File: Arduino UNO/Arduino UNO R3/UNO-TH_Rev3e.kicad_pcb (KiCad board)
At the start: 2 copper layers, 68.6 x 53.3 mm, 120 parts, among them T1 FDN340P, U1 NCP1117ST50T3G, U2 LP2985-33DBVR, U3 ATMEGA16U2-MU(R), U5 LMV358IDGKR, X1 POWERSUPPLY_DC21MMX, X2 USB-B_TH, Y1 16MHz, Y2 CSTCE16M0V53-R0 16MHZ

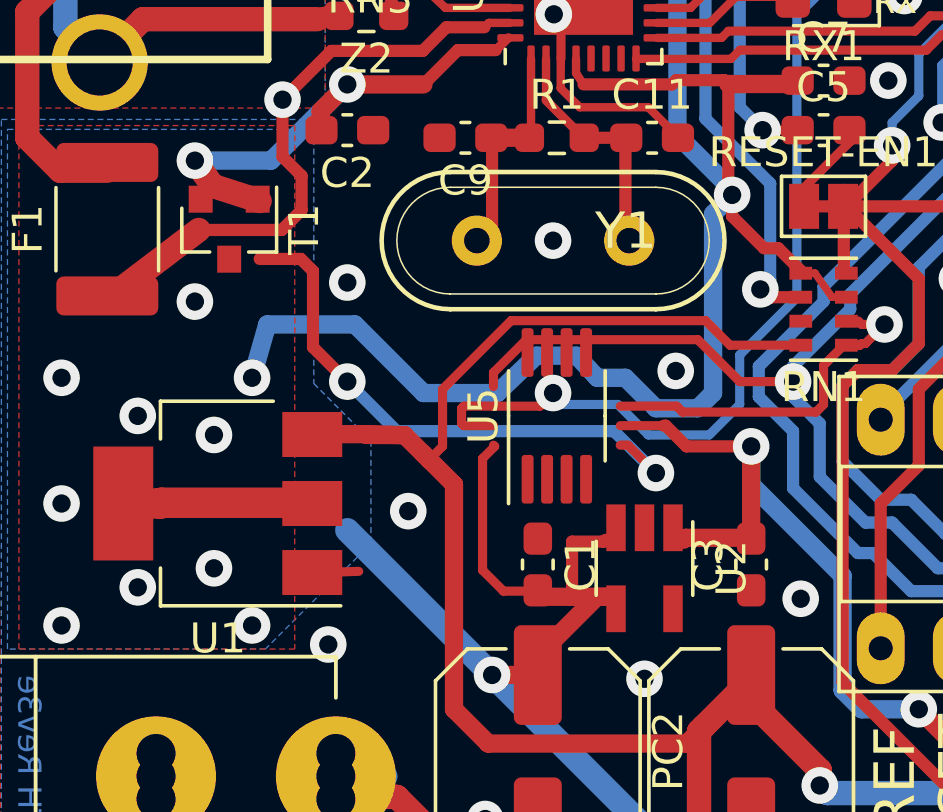
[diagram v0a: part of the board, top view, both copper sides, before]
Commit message: Reoriented some components
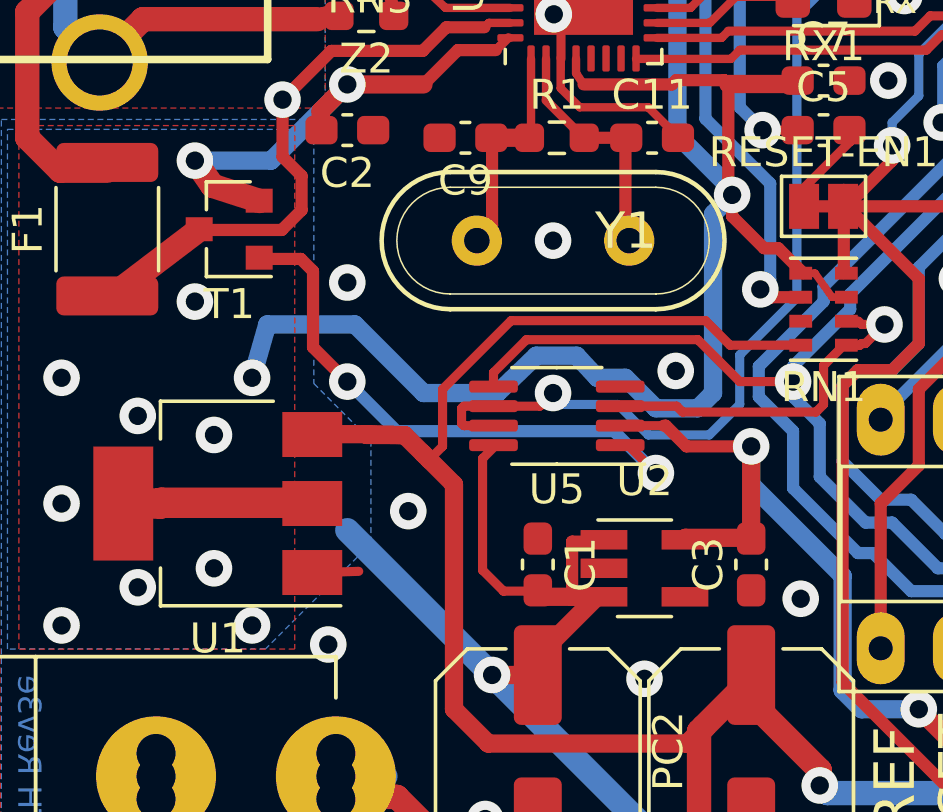
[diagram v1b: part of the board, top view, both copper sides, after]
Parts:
- turned T1 to 180 degrees
- turned U2 to 0 degrees
- turned U5 to 180 degrees
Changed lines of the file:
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@@
   )
   (footprint "Package_TO_SOT_SMD:SOT-23" (layer "F.Cu")
-    (at 122.3391 105.1306 -90)
+    (at 122.3391 105.1306 180)
     (descr "SOT-23, Standard")
     (tags "SOT-23")
     (attr smd)
-    (fp_text reference "T1" (at 0 -2.5 90) (layer "F.SilkS")
-      (effects (font (size 1 1) (thickness 0.15)))
-    )
-    (fp_text value "FDN340P" (at 0 2.5 90) (layer "F.Fab")
-      (effects (font (size 1 1) (thickness 0.15)))
-    )
-    (fp_text user "${REFERENCE}" (at 0 0) (layer "F.Fab")
+    (fp_text reference "T1" (at 0 -2.5) (layer "F.SilkS")
+      (effects (font (size 1 1) (thickness 0.15)))
+    )
+    (fp_text value "FDN340P" (at 0 2.5) (layer "F.Fab")
+      (effects (font (size 1 1) (thickness 0.15)))
+    )
+    (fp_text user "${REFERENCE}" (at 0 0 90) (layer "F.Fab")
       (effects (font (size 0.5 0.5) (thickness 0.075)))
     )
@@
     (fp_line (start -0.7 -0.95) (end -0.15 -1.52) (layer "F.Fab") (width 0.1))
     (fp_line (start -0.7 1.52) (end 0.7 1.52) (layer "F.Fab") (width 0.1))
-    (pad "1" smd rect locked (at -1 -0.95 270) (size 0.9 0.8) (layers "F.Cu" "F.Paste" "F.Mask")
+    (pad "1" smd rect locked (at -1 -0.95 180) (size 0.9 0.8) (layers "F.Cu" "F.Paste" "F.Mask")
       (net 40 "/USBVCC"))
-    (pad "2" smd rect locked (at -1 0.95 270) (size 0.9 0.8) (layers "F.Cu" "F.Paste" "F.Mask")
-      (net 1 "+5V"))
-    (pad "3" smd rect locked (at 1 0 270) (size 0.9 0.8) (layers "F.Cu" "F.Paste" "F.Mask")
+    (pad "2" smd rect locked (at -1 0.95 180) (size 0.9 0.8) (layers "F.Cu" "F.Paste" "F.Mask")
+      (net 1 "+5V"))
+    (pad "3" smd rect locked (at 1 0 180) (size 0.9 0.8) (layers "F.Cu" "F.Paste" "F.Mask")
       (net 41 "/GATE_CMD"))
     (model "${KICAD6_3DMODEL_DIR}/Package_TO_SOT_SMD.3dshapes/SOT-23.wrl"
@@
   )
   (footprint "Package_SO:MSOP-8_3x3mm_P0.65mm" (layer "F.Cu")
-    (at 133.2611 111.3536 90)
+    (at 133.2611 111.3536 180)
     (descr "MSOP, 8 Pin (https://www.jedec.org/system/files/docs/mo-187F.pdf variant AA), generated with kicad-footprint-generator ipc_gullwing_generator.py")
     (tags "MSOP SO")
     (attr smd)
-    (fp_text reference "U5" (at 0 -2.45 90) (layer "F.SilkS")
-      (effects (font (size 1 1) (thickness 0.15)))
-    )
-    (fp_text value "LMV358IDGKR" (at 0 2.45 90) (layer "F.Fab")
-      (effects (font (size 1 1) (thickness 0.15)))
-    )
-    (fp_text user "${REFERENCE}" (at 0 0 90) (layer "F.Fab")
+    (fp_text reference "U5" (at 0 -2.45) (layer "F.SilkS")
+      (effects (font (size 1 1) (thickness 0.15)))
+    )
+    (fp_text value "LMV358IDGKR" (at 0 2.45) (layer "F.Fab")
+      (effects (font (size 1 1) (thickness 0.15)))
+    )
+    (fp_text user "${REFERENCE}" (at 0 0) (layer "F.Fab")
       (effects (font (size 0.75 0.75) (thickness 0.11)))
     )
@@
     (fp_line (start -1.5 -0.75) (end -0.75 -1.5) (layer "F.Fab") (width 0.1))
     (fp_line (start -1.5 1.5) (end -1.5 -0.75) (layer "F.Fab") (width 0.1))
-    (pad "1" smd roundrect locked (at -2.1125 -0.975 90) (size 1.625 0.4) (layers "F.Cu" "F.Paste" "F.Mask") (roundrect_rratio 0.25)
+    (pad "1" smd roundrect locked (at -2.1125 -0.975 180) (size 1.625 0.4) (layers "F.Cu" "F.Paste" "F.Mask") (roundrect_rratio 0.25)
       (net 41 "/GATE_CMD"))
-    (pad "2" smd roundrect locked (at -2.1125 -0.325 90) (size 1.625 0.4) (layers "F.Cu" "F.Paste" "F.Mask") (roundrect_rratio 0.25)
+    (pad "2" smd roundrect locked (at -2.1125 -0.325 180) (size 1.625 0.4) (layers "F.Cu" "F.Paste" "F.Mask") (roundrect_rratio 0.25)
       (net 73 "/+3V3"))
-    (pad "3" smd roundrect locked (at -2.1125 0.325 90) (size 1.625 0.4) (layers "F.Cu" "F.Paste" "F.Mask") (roundrect_rratio 0.25)
+    (pad "3" smd roundrect locked (at -2.1125 0.325 180) (size 1.625 0.4) (layers "F.Cu" "F.Paste" "F.Mask") (roundrect_rratio 0.25)
       (net 68 "/CMP"))
-    (pad "4" smd roundrect locked (at -2.1125 0.975 90) (size 1.625 0.4) (layers "F.Cu" "F.Paste" "F.Mask") (roundrect_rratio 0.25)
-      (net 2 "GND"))
-    (pad "5" smd roundrect locked (at 2.1125 0.975 90) (size 1.625 0.4) (layers "F.Cu" "F.Paste" "F.Mask") (roundrect_rratio 0.25)
+    (pad "4" smd roundrect locked (at -2.1125 0.975 180) (size 1.625 0.4) (layers "F.Cu" "F.Paste" "F.Mask") (roundrect_rratio 0.25)
+      (net 2 "GND"))
+    (pad "5" smd roundrect locked (at 2.1125 0.975 180) (size 1.625 0.4) (layers "F.Cu" "F.Paste" "F.Mask") (roundrect_rratio 0.25)
       (net 12 "/SCK"))
-    (pad "6" smd roundrect locked (at 2.1125 0.325 90) (size 1.625 0.4) (layers "F.Cu" "F.Paste" "F.Mask") (roundrect_rratio 0.25)
+    (pad "6" smd roundrect locked (at 2.1125 0.325 180) (size 1.625 0.4) (layers "F.Cu" "F.Paste" "F.Mask") (roundrect_rratio 0.25)
       (net 67 "/L13"))
-    (pad "7" smd roundrect locked (at 2.1125 -0.325 90) (size 1.625 0.4) (layers "F.Cu" "F.Paste" "F.Mask") (roundrect_rratio 0.25)
+    (pad "7" smd roundrect locked (at 2.1125 -0.325 180) (size 1.625 0.4) (layers "F.Cu" "F.Paste" "F.Mask") (roundrect_rratio 0.25)
       (net 67 "/L13"))
-    (pad "8" smd roundrect locked (at 2.1125 -0.975 90) (size 1.625 0.4) (layers "F.Cu" "F.Paste" "F.Mask") (roundrect_rratio 0.25)
+    (pad "8" smd roundrect locked (at 2.1125 -0.975 180) (size 1.625 0.4) (layers "F.Cu" "F.Paste" "F.Mask") (roundrect_rratio 0.25)
       (net 1 "+5V"))
     (model "${KICAD6_3DMODEL_DIR}/Package_SO.3dshapes/MSOP-8_3x3mm_P0.65mm.wrl"
@@
   )
   (footprint "Package_TO_SOT_SMD:SOT-23-5_HandSoldering" (layer "F.Cu")
-    (at 136.1821 116.4336 -90)
+    (at 136.1821 116.4336)
     (descr "5-pin SOT23 package")
     (tags "SOT-23-5 hand-soldering")
     (attr smd)
-    (fp_text reference "U2" (at 0 -2.9 90) (layer "F.SilkS")
-      (effects (font (size 1 1) (thickness 0.15)))
-    )
-    (fp_text value "LP2985-33DBVR" (at 0 2.9 90) (layer "F.Fab")
-      (effects (font (size 1 1) (thickness 0.15)))
-    )
-    (fp_text user "${REFERENCE}" (at 0 0) (layer "F.Fab")
+    (fp_text reference "U2" (at 0 -2.9) (layer "F.SilkS")
+      (effects (font (size 1 1) (thickness 0.15)))
+    )
+    (fp_text value "LP2985-33DBVR" (at 0 2.9) (layer "F.Fab")
+      (effects (font (size 1 1) (thickness 0.15)))
+    )
+    (fp_text user "${REFERENCE}" (at 0 0 90) (layer "F.Fab")
       (effects (font (size 0.5 0.5) (thickness 0.075)))
     )
@@
     (fp_line (start 0.9 -1.55) (end -0.25 -1.55) (layer "F.Fab") (width 0.1))
     (fp_line (start -0.9 -0.9) (end -0.9 1.55) (layer "F.Fab") (width 0.1))
-    (pad "1" smd rect locked (at -1.35 -0.95 270) (size 1.56 0.65) (layers "F.Cu" "F.Paste" "F.Mask")
-      (net 1 "+5V"))
-    (pad "2" smd rect locked (at -1.35 0 270) (size 1.56 0.65) (layers "F.Cu" "F.Paste" "F.Mask")
-      (net 2 "GND"))
-    (pad "3" smd rect locked (at -1.35 0.95 270) (size 1.56 0.65) (layers "F.Cu" "F.Paste" "F.Mask")
-      (net 1 "+5V"))
-    (pad "4" smd rect locked (at 1.35 0.95 270) (size 1.56 0.65) (layers "F.Cu" "F.Paste" "F.Mask")
+    (pad "1" smd rect locked (at -1.35 -0.95) (size 1.56 0.65) (layers "F.Cu" "F.Paste" "F.Mask")
+      (net 1 "+5V"))
+    (pad "2" smd rect locked (at -1.35 0) (size 1.56 0.65) (layers "F.Cu" "F.Paste" "F.Mask")
+      (net 2 "GND"))
+    (pad "3" smd rect locked (at -1.35 0.95) (size 1.56 0.65) (layers "F.Cu" "F.Paste" "F.Mask")
+      (net 1 "+5V"))
+    (pad "4" smd rect locked (at 1.35 0.95) (size 1.56 0.65) (layers "F.Cu" "F.Paste" "F.Mask")
       (net 74 "Net-(U2-Pad4)"))
-    (pad "5" smd rect locked (at 1.35 -0.95 270) (size 1.56 0.65) (layers "F.Cu" "F.Paste" "F.Mask")
+    (pad "5" smd rect locked (at 1.35 -0.95) (size 1.56 0.65) (layers "F.Cu" "F.Paste" "F.Mask")
       (net 73 "/+3V3"))
     (model "${KICAD6_3DMODEL_DIR}/Package_TO_SOT_SMD.3dshapes/SOT-23-5.wrl"
